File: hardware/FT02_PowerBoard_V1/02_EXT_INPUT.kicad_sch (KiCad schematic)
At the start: 0 parts

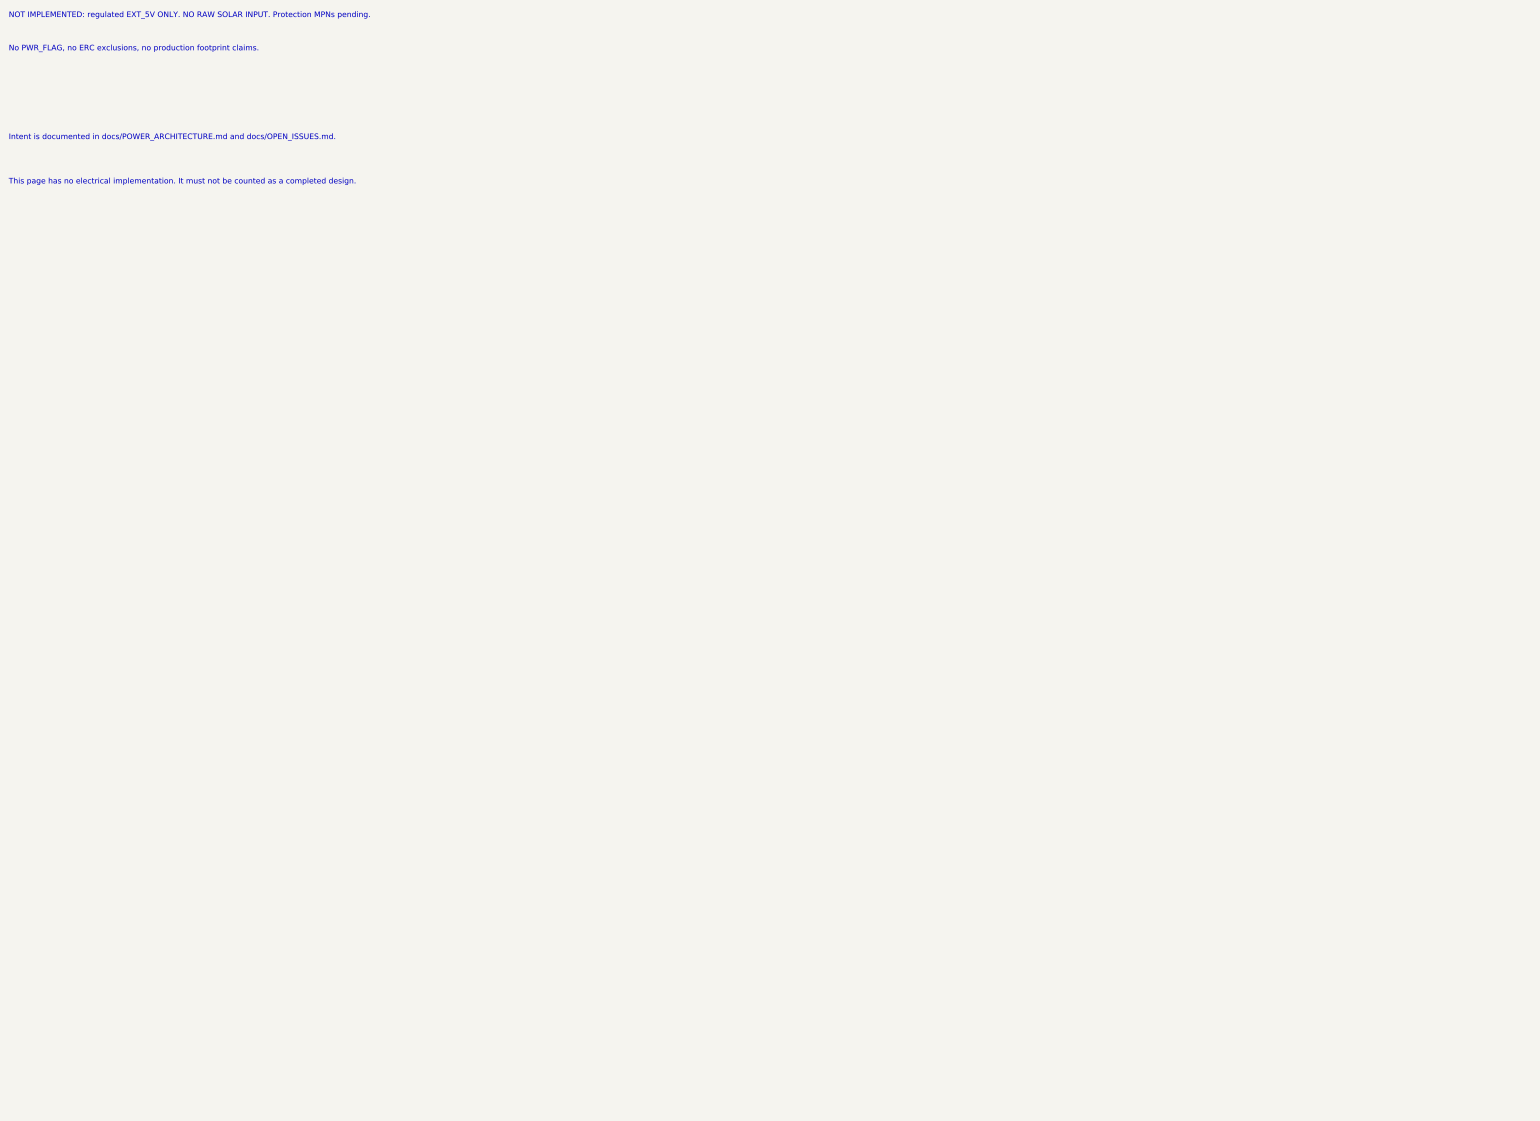
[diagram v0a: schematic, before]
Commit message: Add unqualified FT02 EXT input guard and tolerance checks
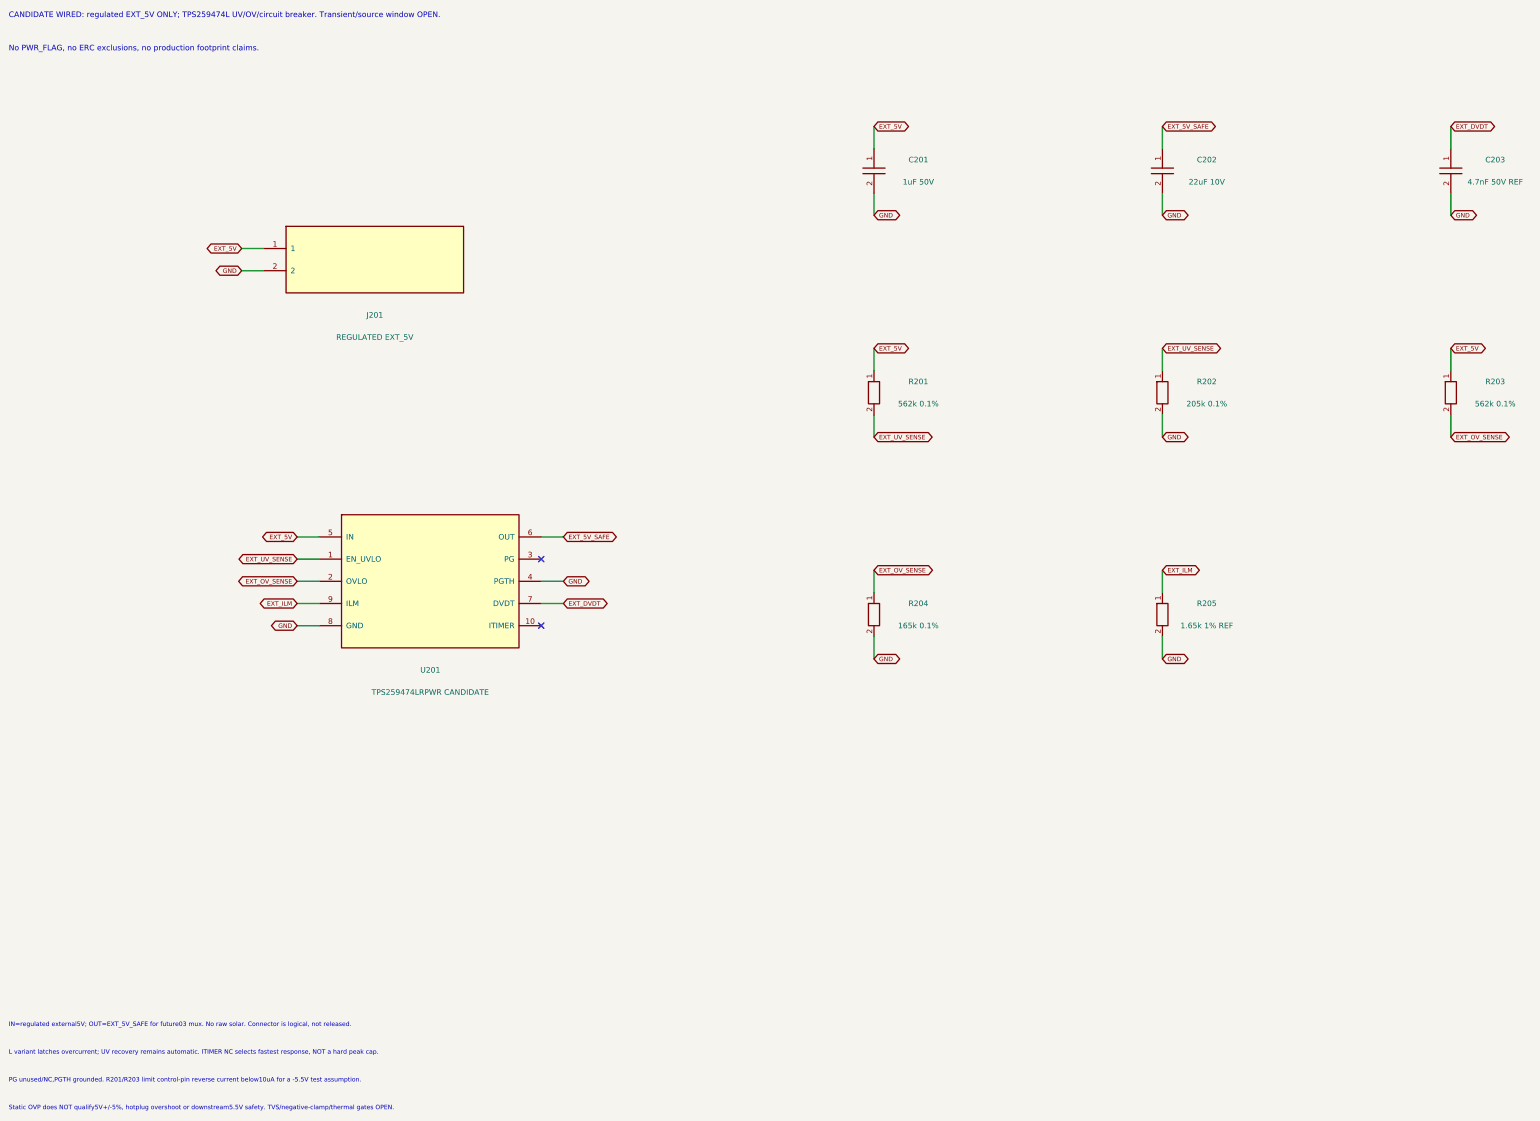
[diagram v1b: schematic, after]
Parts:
- added C201: 1uF 50V, symbol FT02_Reference:C
- added C202: 22uF 10V, symbol FT02_Reference:C
- added C203: 4.7nF 50V REF, symbol FT02_Reference:C
- added J201: REGULATED EXT_5V, symbol FT02_Reference:CONN2
- added R201, R203: 562k 0.1%, symbol FT02_Reference:R
- added R202: 205k 0.1%, symbol FT02_Reference:R
- added R204: 165k 0.1%, symbol FT02_Reference:R
- added R205: 1.65k 1% REF, symbol FT02_Reference:R
- added U201: TPS259474LRPWR CANDIDATE, symbol FT02_Reference:TPS259474
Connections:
- new net EXT_5V: C201.1, J201.1, R201.1, R203.1, U201.5 (IN)
- new net EXT_5V_SAFE: C202.1, U201.6 (OUT)
- new net EXT_DVDT: C203.1, U201.7 (DVDT)
- new net EXT_ILM: R205.1, U201.9 (ILM)
- new net EXT_OV_SENSE: R203.2, R204.1, U201.2 (OVLO)
- new net EXT_UV_SENSE: R201.2, R202.1, U201.1 (EN_UVLO)
- new net GND: C201.2, C202.2, C203.2, J201.2, R202.2, R204.2, R205.2, U201.4 (PGTH), U201.8 (GND)
- no-connect marks 0 -> 2
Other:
- note added: "CANDIDATE WIRED: regulated EXT_5V ONLY; TPS259474L UV/OV/circuit breaker. Transient/source window OPEN."
- note added: "IN=regulated external5V; OUT=EXT_5V_SAFE for future03 mux. No raw solar. Connector is logical, not released."
- note added: "L variant latches overcurrent; UV recovery remains automatic. ITIMER NC selects fastest response, NOT a hard peak cap."
- note added: "PG unused/NC,PGTH grounded. R201/R203 limit control-pin reverse current below10uA for a -5.5V test assumption."
- note added: "Static OVP does NOT qualify5V+/-5%, hotplug overshoot or downstream5.5V safety. TVS/negative-clamp/thermal gates OPEN."
- note removed: "Intent is documented in docs/POWER_ARCHITECTURE.md and docs/OPEN_ISSUES.md."
- note removed: "NOT IMPLEMENTED: regulated EXT_5V ONLY. NO RAW SOLAR INPUT. Protection MPNs pending."
- note removed: "This page has no electrical implementation. It must not be counted as a completed design."
